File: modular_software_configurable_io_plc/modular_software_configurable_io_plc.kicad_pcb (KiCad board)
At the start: 4 copper layers, 105 x 107 mm, 29 parts, among them J1 FW-14-03-G-D-085-155, J10 CLP-108-02-G-D-BE, J11 CLP-102-02-G-D-BE, J12 CLP-102-02-G-D-BE, J13 CLP-102-02-G-D-BE, J14 CLP-108-02-G-D-BE, J15 FW-14-03-G-D-085-155, J16 FW-02-03-G-D-085-155, J17 FW-02-03-G-D-085-155, J18 FW-02-03-G-D-085-155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

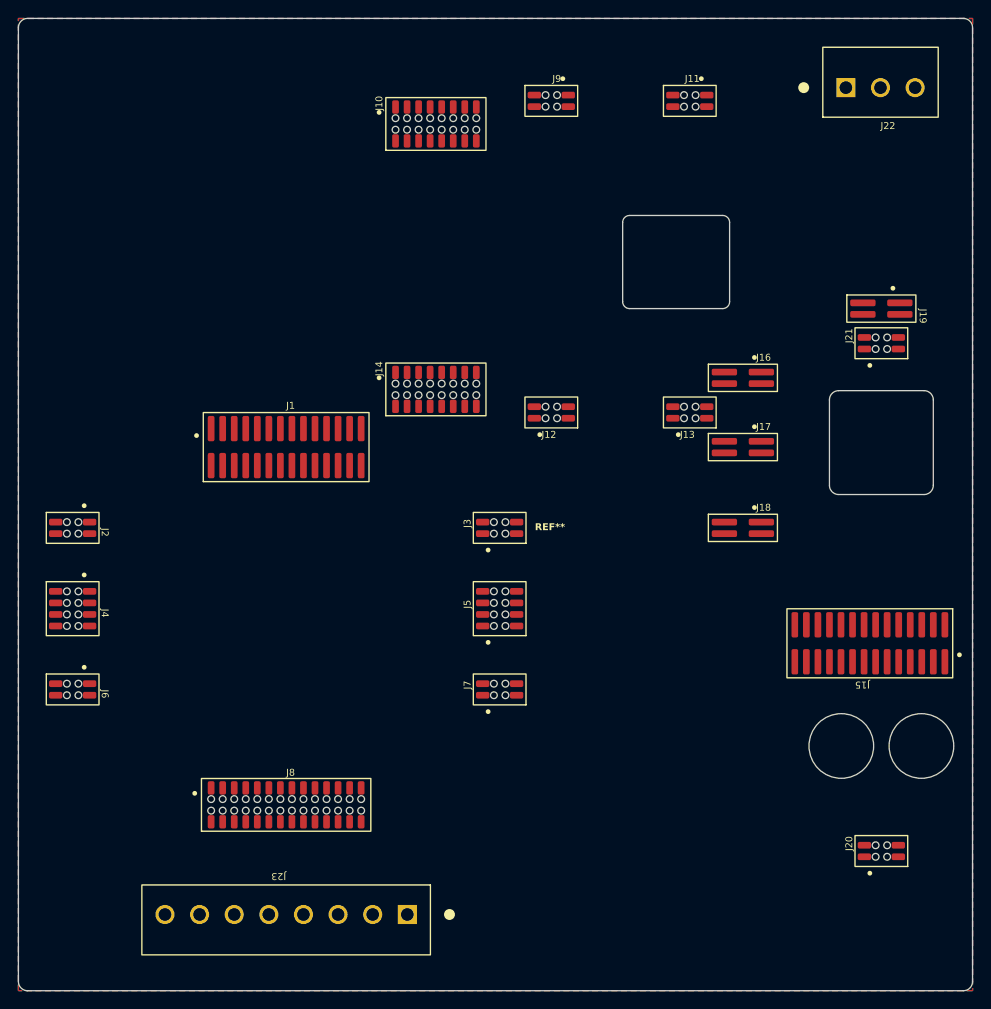
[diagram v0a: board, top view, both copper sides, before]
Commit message: Update KiCAD Symbol Generator submodule to latest commit
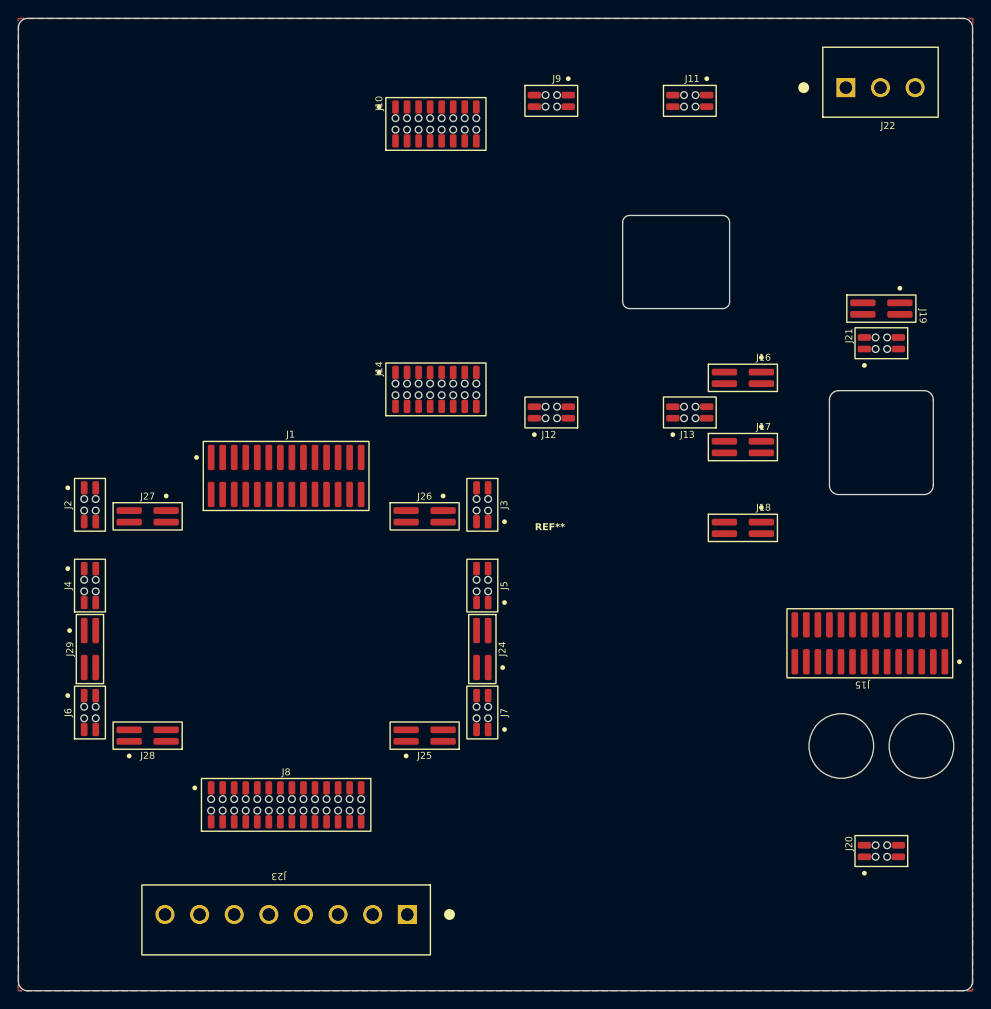
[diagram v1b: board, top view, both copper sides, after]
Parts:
- added J24: FW-02-03-G-D-085-155, connector_footprints:FW-02-03-G-D-085-155, F.Cu at (176.3, 109.6)
- added J25: FW-02-03-G-D-085-155, connector_footprints:FW-02-03-G-D-085-155, F.Cu at (169.9, 119.1)
- added J26: FW-02-03-G-D-085-155, connector_footprints:FW-02-03-G-D-085-155, F.Cu at (169.9, 95.0)
- added J27: FW-02-03-G-D-085-155, connector_footprints:FW-02-03-G-D-085-155, F.Cu at (139.4, 95.0)
- added J28: FW-02-03-G-D-085-155, connector_footprints:FW-02-03-G-D-085-155, F.Cu at (139.4, 119.1)
- added J29: FW-02-03-G-D-085-155, connector_footprints:FW-02-03-G-D-085-155, F.Cu at (133.1, 109.6)
- J22: value TBP02R2-381-03BE -> TBP02R2-381
- J23: value TBP02R2-381-08BE -> TBP02R2-381
- J4, J5: value CLP-104-02-G-D-BE -> CLP-102-02-G-D-BE; footprint connector_footprints:CLP-104-02-G-D-BE -> connector_footprints:CLP-102-02-G-D-BE
- moved MOD2 4.44 mm to (154.7, 109.6)
- moved J2 3.18 mm to (133.1, 93.7), turned to 0 degrees
- moved J3 3.18 mm to (176.3, 93.7), turned to 180 degrees
- moved J4 3.18 mm to (133.1, 102.6), turned to 0 degrees
- moved J5 3.18 mm to (176.3, 102.6), turned to 180 degrees
- moved J1 3.17 mm to (154.7, 90.6)
- moved J6 3.17 mm to (133.1, 116.6), turned to 0 degrees
- moved J7 3.17 mm to (176.3, 116.6), turned to 180 degrees

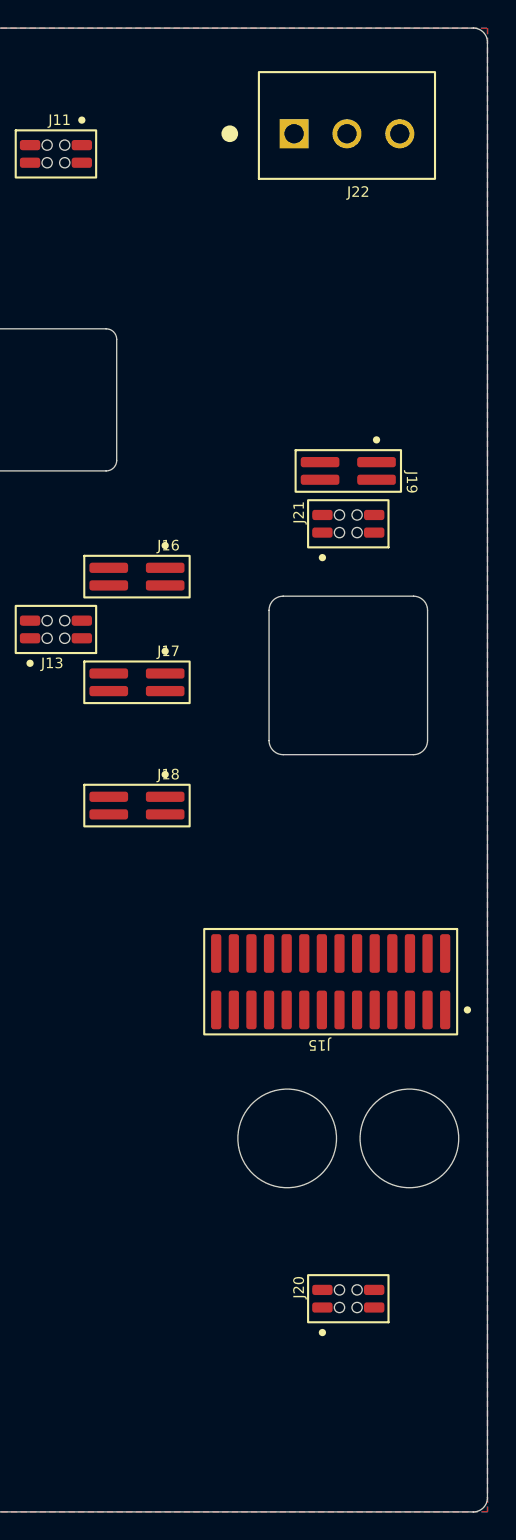
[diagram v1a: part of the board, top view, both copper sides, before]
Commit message: Update KiCAD Symbol Generator submodule to latest commit
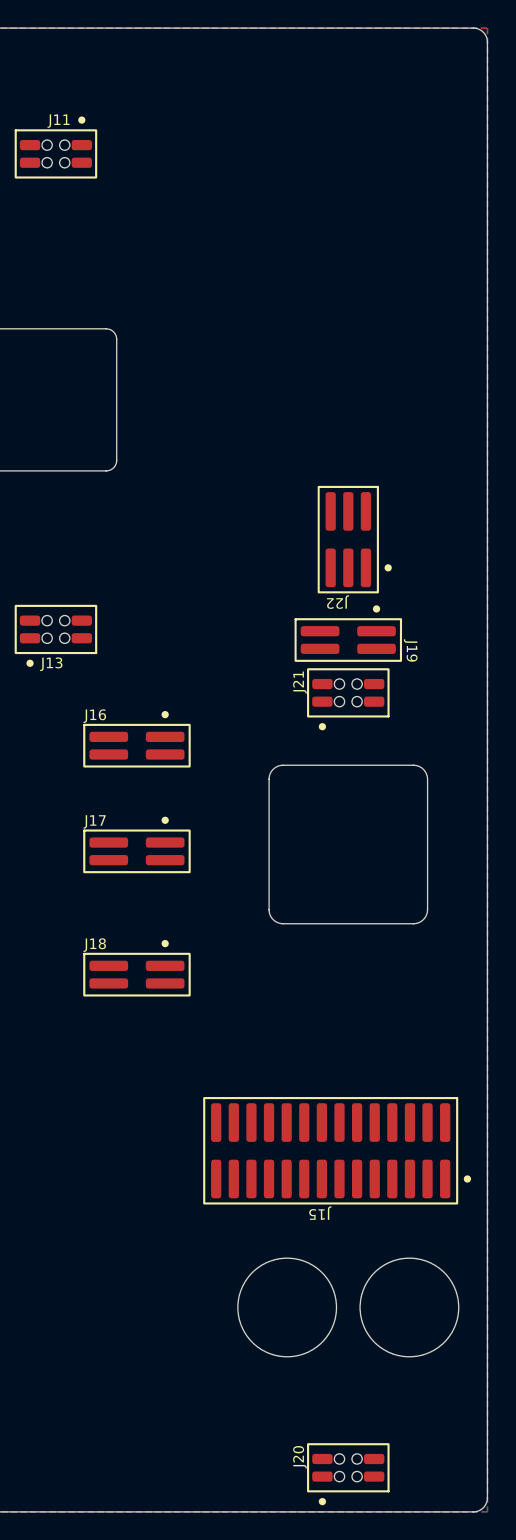
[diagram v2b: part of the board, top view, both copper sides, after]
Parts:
- added MOD6: ~, modules_footprints:minimal_spoe_hybrid, F.Cu at (220.2, 57.7)
- J22: value TBP02R2-381 -> FW-03-03-G-D-085-155; footprint connector_footprints:TBP02R2-381-03BE -> connector_footprints:FW-03-03-G-D-085-155
- J23: value TBP02R2-381 -> TBP02R2-381-08BE
- moved J22 29.3 mm to (220.2, 77.1), turned to 180 degrees
- moved J15 12.2 mm to (218.9, 121.2)
- moved J19 12.2 mm to (220.2, 84.3)
- moved J20 12.2 mm to (220.2, 144.0)
- moved J21 12.2 mm to (220.2, 88.1)
- moved MOD4 12.2 mm to (218.9, 105.3)
- moved MOD5 12.2 mm to (220.2, 115.0)
- moved J16 12.2 mm to (204.9, 91.9)
- moved J17 12.2 mm to (204.9, 99.6)
- moved J18 12.2 mm to (204.9, 108.5)

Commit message: Backup
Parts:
- J21: footprint connector_footprints:CLP-102-02-G-D-BE -> connector_footprints:CLP-103-02-G-D-BE
- moved J21 5.60 mm to (215.1, 85.8), turned to 180 degrees
- moved MOD5 5.09 mm to (215.1, 115.3)
- moved J17 3.62 mm to (204.9, 103.2), turned to 0 degrees
- moved J16 2.98 mm to (204.9, 94.9), turned to 0 degrees
- moved J15 2.98 mm to (218.9, 124.1)
- moved J18 2.98 mm to (204.9, 111.4), turned to 0 degrees
- moved MOD4 2.98 mm to (218.9, 108.3)
- moved J19 2.62 mm to (221.3, 86.7), turned to 180 degrees
- moved J20 0.83 mm to (220.2, 143.2)
- moved J22 0.38 mm to (220.6, 77.1)
- moved MOD6 0.38 mm to (220.6, 57.7)
